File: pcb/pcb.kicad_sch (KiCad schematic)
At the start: 46 parts, among them J1 Conn_02x08_Top_Bottom, J2 Conn_02x08_Top_Bottom, SW1 CherryMX_LED, SW2 CherryMX_LED, SW3 1241.1100.7095, SW4 SW_SPST, U1 ICM7211AMIPL, U2 ICM7211AMIPL, U3 ATTINY84A, U4 NL37WZ14USG, U5 SN74AHC138DR, U6 MAX5035BUSA+, U6 SN74F02D, U7 TC7WZ32FK_LJCT, Y1 Crystal

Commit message: initialize pcb design
Signed-off-by: Michael Darr <michael.e.darr@gmail.com>
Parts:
- BT1: value Battery -> ~9V; footprint (none) -> Connector_Wire:SolderWire-0.15sqmm_1x02_P4mm_D0.5mm_OD1.5mm; Capacity ~5Ah -> (none); Cells 6 * AAA -> (none); Manufacturer_Name (none) -> Memory Protection Devices, Inc; Notes (none) -> 6 AAA batteries, ~9Ah; PN (none) -> BH26AAAW; Volatage ~12V -> (none)
- C1, C2, C3, C4, C5, C6, C7: footprint (none) -> chess_clock:RDER71H104K0M1H03A; Capacitance (none) -> 0.1µF; Manufacturer_Name (none) -> Murata; Notes (none) -> Ceramic Capacitor; PN (none) -> RDER71H104K0M1H03A
- C10: value C -> 0.1µF; footprint (none) -> chess_clock:RDER71H104K0M1H03A; Manufacturer_Name (none) -> Murata; Notes datasheet, pg 12: "Use a 1µF or greater value ceramic capac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 -> Ceramic Capacitor; PN (none) -> RDER71H104K0M1H03A; Type ceramic -> (none)
- C11: renamed from C7; value C -> 0.1µF; footprint (none) -> chess_clock:RDER71H104K0M1H03A; Manufacturer_Name (none) -> Murata; Notes (none) -> Ceramic Capacitor; PN (none) -> RDER71H104K0M1H03A; Spec page 9: "Bypass VD to GND with a 0.1µF ceramic capacitor." -> (none); Type ceramic -> (none)
- C12: renamed from C6; value C_Polarized_Small_US -> 68µF; footprint (none) -> chess_clock:TPSD686K010R0100; Manufacturer_Name (none) -> KYOCERA AVX; Notes (none) -> Polarized Capacitor; PN (none) -> TPSD686K010R0100
- C13: renamed from C11; value C -> 11pF; footprint (none) -> chess_clock:GJM1555C1H110FB01D; Capacitance 20pF -> 11pF; Manufacturer_Name (none) -> Murata; Notes (none) -> Ceramic Capacitor; PN (none) -> GJM1555C1H110FB01D
- C14: renamed from C12; value C -> 11pF; footprint (none) -> chess_clock:GJM1555C1H110FB01D; Capacitance 20pF -> 11pF; Manufacturer_Name (none) -> Murata; Notes (none) -> Ceramic Capacitor; PN (none) -> GJM1555C1H110FB01D
- C8: value C -> 0.1µF; footprint (none) -> chess_clock:RDER71H104K0M1H03A; Manufacturer_Name (none) -> Murata; Notes (none) -> Ceramic Capacitor; PN (none) -> RDER71H104K0M1H03A; Spec pg. 9: "Connect a 0.1µF ceramic capacitor from BST to LX." -> (none); Type ceramic -> (none)
- C9: value C_Polarized_Small_US -> 68µF; footprint (none) -> chess_clock:TPSD686K010R0100; Manufacturer_Name (none) -> KYOCERA AVX; Notes TODO => calculate precise capacitance (pg. 11/12) -> Polarized Capacitor; PN (none) -> TPSD686K010R0100
- D1: value D_Schottky -> Schottky Diode; footprint (none) -> chess_clock:B240AE-13; Manufacturer_Name (none) -> Diodes Inc.; Notes (none) -> Schottky Diode | page 11, table 1, 7.5 to 36; PN (none) -> B240AE-13; PN - Central Semiconductor B240 -> (none); PN - Diodes, Inc B240A -> (none); PN - IR 15MQ040N -> (none); PN - ON Semiconductor MBRS240, MBRS1540 -> (none); Spec page 11, table 1, 7.5 to 36 (PN recommendations reproduced 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 -> (none)
- FET1, FET2: value XP9561GI -> PMOS; footprint (none) -> Package_TO_SOT_THT:TO-220-3_Vertical; Manufacturer_Name (none) -> Yageo; PN (none) -> XP9561GI
- J1, J2: value Conn_02x08_Top_Bottom -> Dubugging Headers; footprint (none) -> chess_clock:10129381-916001BLF; Manufacturer_Name (none) -> Amphenol; PN (none) -> 10129381-916001BLF
- L1: value L -> 100μH; footprint (none) -> chess_clock:DO5022P-104MLD; Inductance 100μH -> (none); Manufacturer_Name (none) -> Coilcraft; PN (none) -> DO5022P-104MLD
- LCD1, LCD2: footprint DIP4000W30P254L6985H218Q40N -> chess_clock:LCD-S401C71TR; Arrow Part Number LCD-S401C71TR -> (none); Arrow Price/Stock https://www.arrow.com/en/products/lcd-s401c71tr/lumex -> (none); Height 2.18 -> (none); Manufacturer_Part_Number LCD-S401C71TR -> (none); Mouser Part Number 696-LCD-S401C71TR -> (none); Mouser Price/Stock https://www.mouser.co.uk/ProductDetail/Lumex/LCD-S401C71TR?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 -> (none); PN (none) -> LCD-S401C71TR
- LED1: value 151033RS03000 -> Red low battery Indicator; footprint (none) -> LED_THT:LED_D3.0mm_Clear; Manufacturer_Name (none) -> Wurth Elektronik; PN (none) -> 151033RS03000
- LS1: footprint (none) -> chess_clock:CT-1205H-SMT; Manufacturer_Name (none) -> CUI Devices; PN (none) -> CT-1205H-SMT-TR
- R1, R2, R3: footprint (none) -> Resistor_THT:R_Axial_DIN0204_L3.6mm_D1.6mm_P2.54mm_Vertical; Manufacturer_Name (none) -> TE connectivity; PN (none) -> ROX1SJ100R
- R4: footprint (none) -> Resistor_THT:R_Axial_DIN0204_L3.6mm_D1.6mm_P2.54mm_Vertical; Manufacturer_Name (none) -> TE connectivity; PN (none) -> CFR16J4K7
- R5: footprint (none) -> Resistor_THT:R_Axial_DIN0204_L3.6mm_D1.6mm_P2.54mm_Vertical; Manufacturer_Name (none) -> TE connectivity; PN (none) -> CFR50J5K6
- R6, R7, R8: footprint (none) -> Resistor_THT:R_Axial_DIN0204_L3.6mm_D1.6mm_P2.54mm_Vertical; Manufacturer_Name (none) -> TE connectivity; PN (none) -> ROX1SJ100K
- SW1, SW2: value CherryMX_LED -> Cherry MX Grey Switch w/ Green LED; footprint (none) -> chess_clock:MX_LED; Manufacturer_Name (none) -> Cherry; Notes (none) -> LED PN: INL-3AG30 [datasheet](https://www.inolux-corp.com/d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; PN (none) -> MX1A-D1NA
- SW3: footprint (none) -> chess_clock:MCS 18 Front; Manufacturer_Name (none) -> Schurter; PN (none) -> 1241.1100.7095
- SW4: footprint (none) -> chess_clock:CWSA11AAN1H; Manufacturer_Name (none) -> NKK Switches; PN (none) -> CWSA11AAN1H
- U1, U2: value ICM7211AMIPL -> Display Driver; footprint 21-0044B_40_MXM -> chess_clock:ICM7211AMIPL; Manufacturer_Name (none) -> Maxim; PN (none) -> ICM7211AMIPL
- U3: value ATTINY84A -> MCU; footprint DIP794W56P254L1918H533Q14N -> chess_clock:ATtiny84a; Height 5.334 -> (none); Manufacturer_Part_Number ATTINY48A-PU -> (none); PN (none) -> ATTINY84A
- U4: value NL37WZ14USG -> Inverter, 3 Channels; footprint US8_2P40X2P10_ONS -> chess_clock:NL37WZ14USG; Manufacturer_Name (none) -> Onsemi; PN (none) -> NL37WZ14USG
- U5: value SN74AHC138DR -> 3:8 Demux; footprint D16 -> chess_clock:SN74AHC138DR; Manufacturer_Name (none) -> Texas Instruments; PN (none) -> SN74AHC138DR
- U6: value SN74F02D -> NOR, 4 Channels; footprint D14 -> chess_clock:SN74F02D; Manufacturer_Name (none) -> Texas Instruments; PN (none) -> SN74F02D
- U7: value TC7WZ32FK_LJCT -> OR, 2 Channels; footprint US8_TOS -> chess_clock:TC7WZ32FK_LJCT; Manufacturer_Name (none) -> Toshiba; PN (none) -> TC7WZ32FK
- U8: renamed from U6; value MAX5035BUSA+ -> 5V Buck Voltage Regulator; footprint 21-0041B_8_MXM -> chess_clock:MAX5035BUSA+; Manufacturer_Name (none) -> Maxim; PN (none) -> MAX5035BUSA+
- Y1: value Crystal -> 20MHz Crystal; footprint (none) -> chess_clock:ECS_200_18_4X_CKM; Frequency 20MHz -> (none); Manufacturer_Name (none) -> ECS Inc; PN (none) -> ECS-200-18-4X-CKM
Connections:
- net GND: now also C1.1, C2.1, C3.1, SW1.1; no longer C1.2, C2.2, C3.2, SW1.2
- net VCC: now also C1.2, C2.2, C3.2; no longer C1.1, C2.1, C3.1
- net buzz: now also LS1.1 (-), U5.12 (Y3)
- net at R6.1: now also SW1.2; no longer SW1.1
- net col1_disable renamed ~{col1_enable}
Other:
- note removed: "0.5"
- note removed: "12/11/23"
- note removed: "Cn decouples Un"
- note removed: "liclock"
- company: (none) -> Alset
- title: (none) -> Liclock
- moved on the sheet: BT1, C1, C10, C11, C12, C13, C14, C2, C3, C4, C5, C6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
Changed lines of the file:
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@@
 (kicad_sch (version 20230121) (generator eeschema)
   (paper "A4")
+  (title_block
+    (title "Liclock")
+    (date "2023-12-12")
+    (rev "0,6")
+    (company "Alset")
+  )

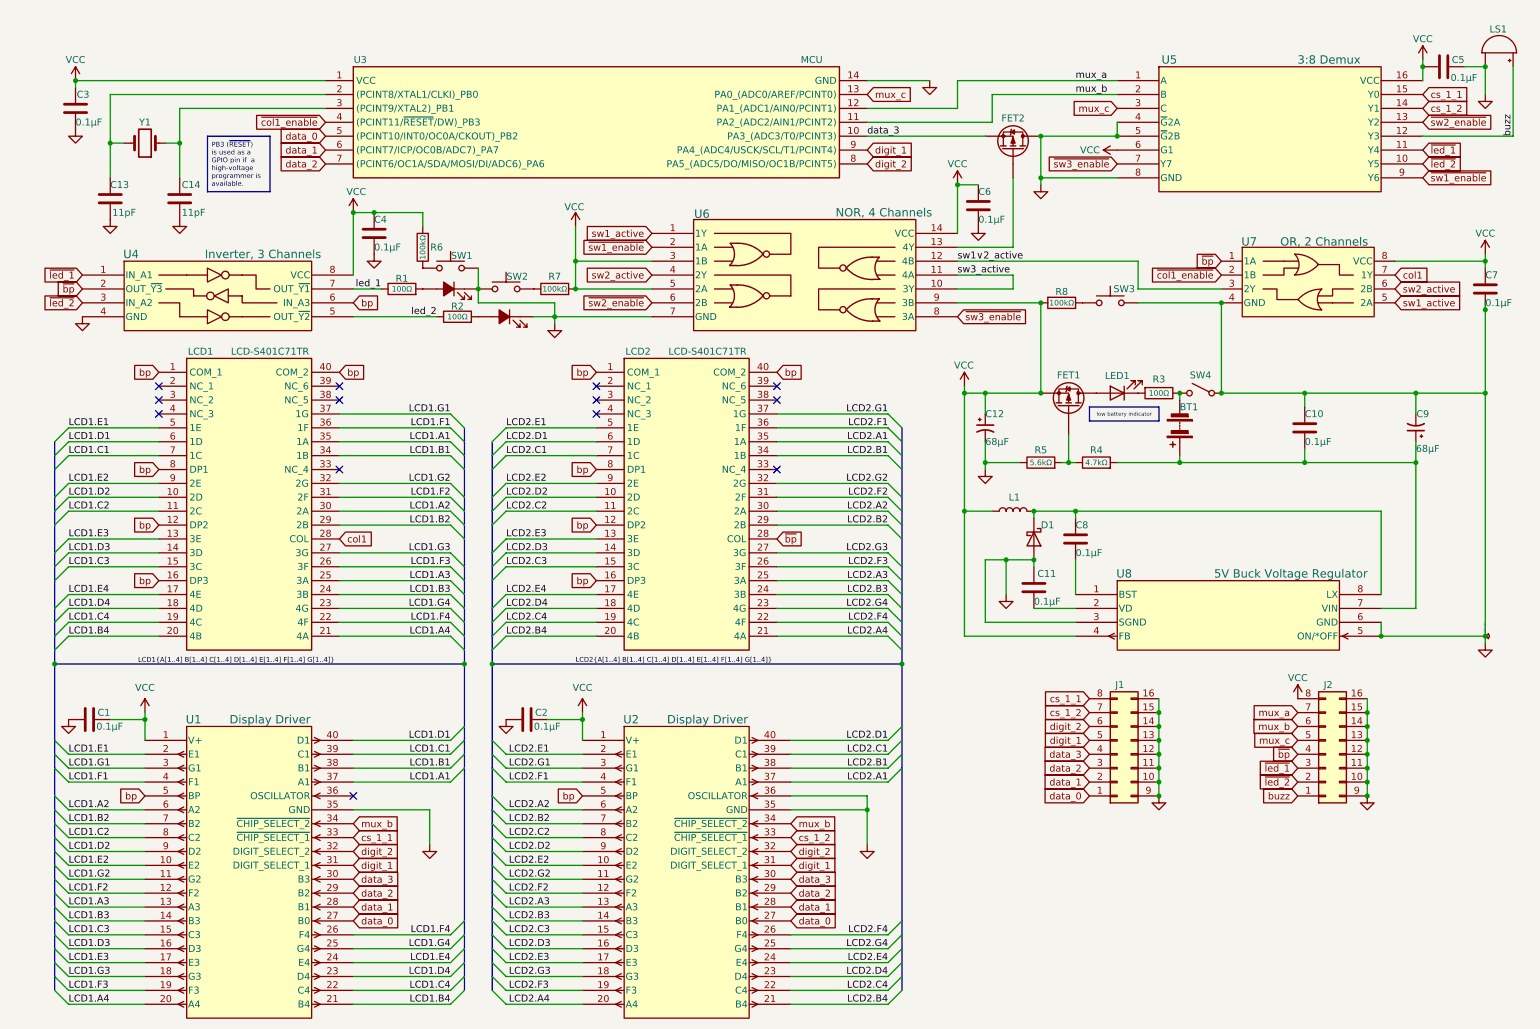
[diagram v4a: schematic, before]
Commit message: begin split pcb layout
Signed-off-by: Michael Darr <michael.e.darr@gmail.com>
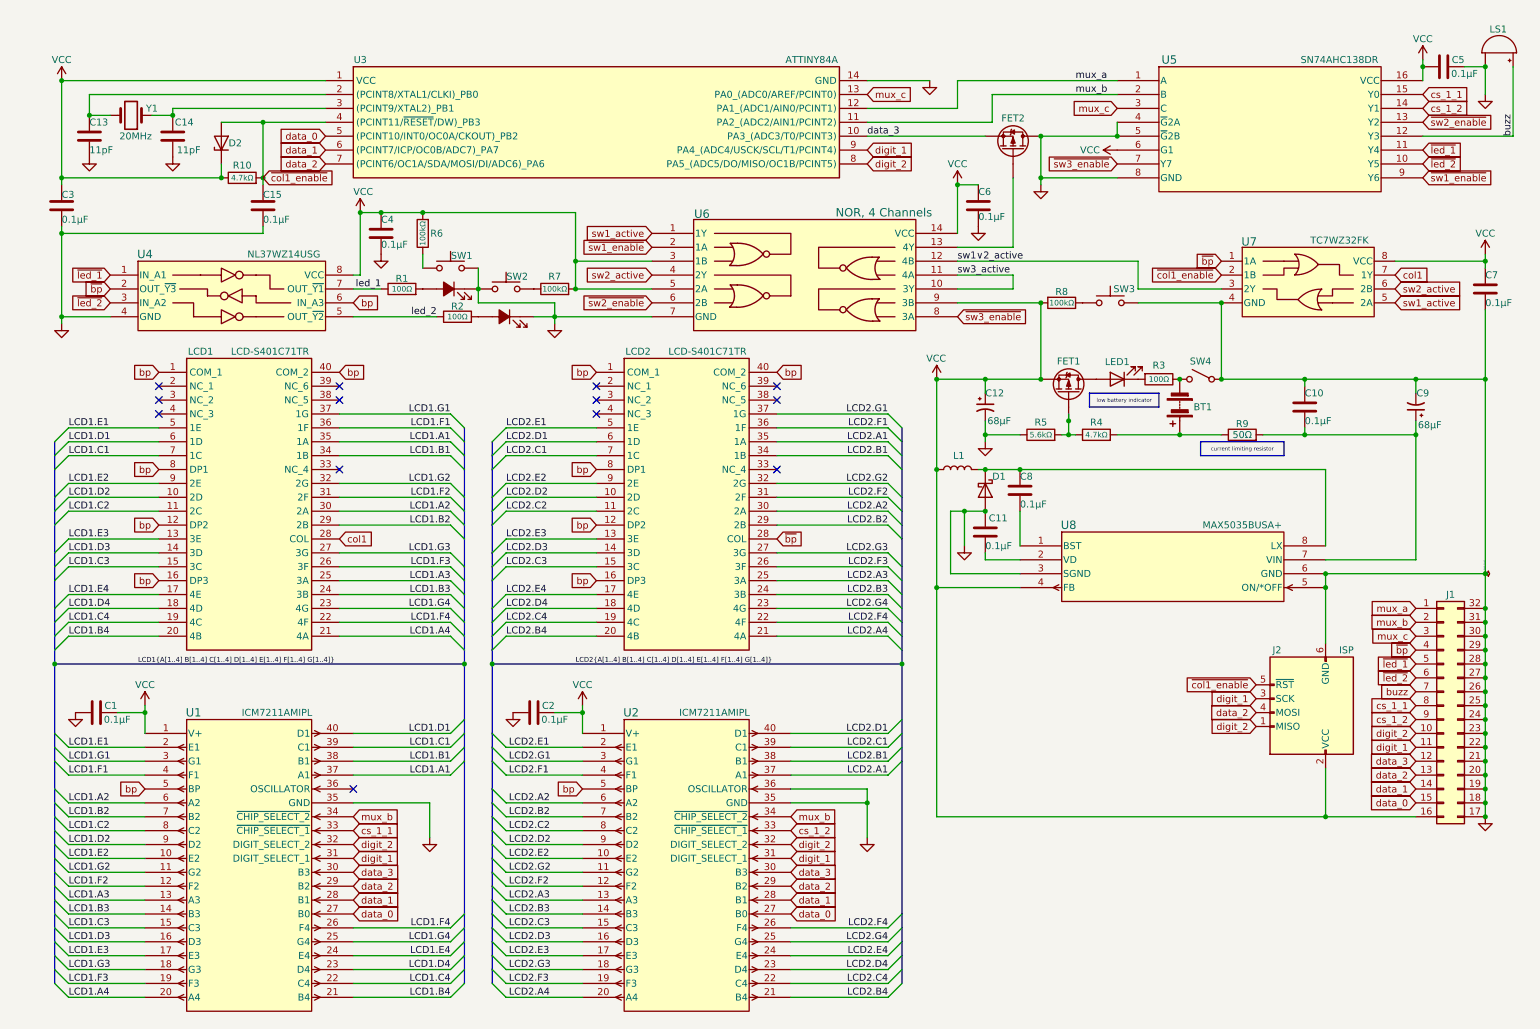
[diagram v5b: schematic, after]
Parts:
- removed J1, J2: Dubugging Headers, chess_clock:10129381-916001BLF, symbol Connector_Generic:Conn_02x08_Top_Bottom
- added C15: 0.1µF, chess_clock:RDER71H104K0M1H03A, symbol Device:C
- added D2: TVS Diode, Diode_SMD:D_SOD-523, symbol Device:D_Zener
- added J1: Debugging, Connector_PinHeader_2.54mm:PinHeader_2x16_P2.54mm_Vertical, symbol Connector_Generic:Conn_02x16_Counter_Clockwise
- added J2: ISP, Connector_PinHeader_2.54mm:PinHeader_2x03_P2.54mm_Vertical, symbol Connector:AVR-ISP-6
- added R10: 4.7kΩ, Resistor_THT:R_Axial_DIN0204_L3.6mm_D1.6mm_P2.54mm_Vertical, symbol Device:R
- added R9: 50Ω, chess_clock:352151RFT, symbol Device:R
- C1, C10, C11, C2, C3, C4, C5, C6, C7, C8: Capacitance 0.1µF -> (none); Notes Ceramic Capacitor -> (none)
- C12, C9: Capacitance 68µF -> (none); Notes Polarized Capacitor -> (none)
- C13, C14: Capacitance 11pF -> (none); Notes Ceramic Capacitor -> (none)
- D1: Notes Schottky Diode | page 11, table 1, 7.5 to 36 -> (none)
- Y1: value 20MHz Crystal -> 20MHz
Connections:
- net GND: now also C15.1, J1.17 (Pin_17), J1.18 (Pin_18), J1.19 (Pin_19), J1.20 (Pin_20), J1.21 (Pin_21), J1.22 (Pin_22), J1.23 (Pin_23), J1.24 (Pin_24), J1.25 (Pin_25), J1.26 (Pin_26), J1.27 (Pin_27), J1.28 (Pin_28), J1.29 (Pin_29), J1.30 (Pin_30), J1.31 (Pin_31), J1.32 (Pin_32), J2.6 (GND)
- net VCC: now also D2.1 (K), J1.16 (Pin_16), J2.2 (VCC), R10.1
- net buzz: now also J1.7 (Pin_7)
- net cs_1_1: now also J1.8 (Pin_8)
- net cs_1_2: now also J1.9 (Pin_9)
- net data_0: now also J1.15 (Pin_15)
- net data_1: now also J1.14 (Pin_14)
- net data_2: now also J1.13 (Pin_13), J2.4 (MOSI)
- net data_3: now also J1.12 (Pin_12)
- net digit_1: now also J1.11 (Pin_11), J2.3 (SCK)
- net digit_2: now also J1.10 (Pin_10), J2.1 (MISO)
- net mux_a: now also J1.1 (Pin_1)
- net mux_b: now also J1.2 (Pin_2)
- net mux_c: now also J1.3 (Pin_3)
- net ~{bp}: now also J1.4 (Pin_4)
- net ~{col1_enable}: now also C15.2, D2.2 (A), J2.5 (~{RST}), R10.2
- net ~{led_1}: now also J1.5 (Pin_5)
- net ~{led_2}: now also J1.6 (Pin_6)
- net at C10.2, C9.1, U8.7 (VIN): now also R9.2; no longer BT1.1 (+), R4.2
- new net: BT1.1 (+), R4.2, R9.1
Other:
- moved on the sheet: BT1, C1, C10, C11, C12, C13, C14, C2, C3, C4, C8, C9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

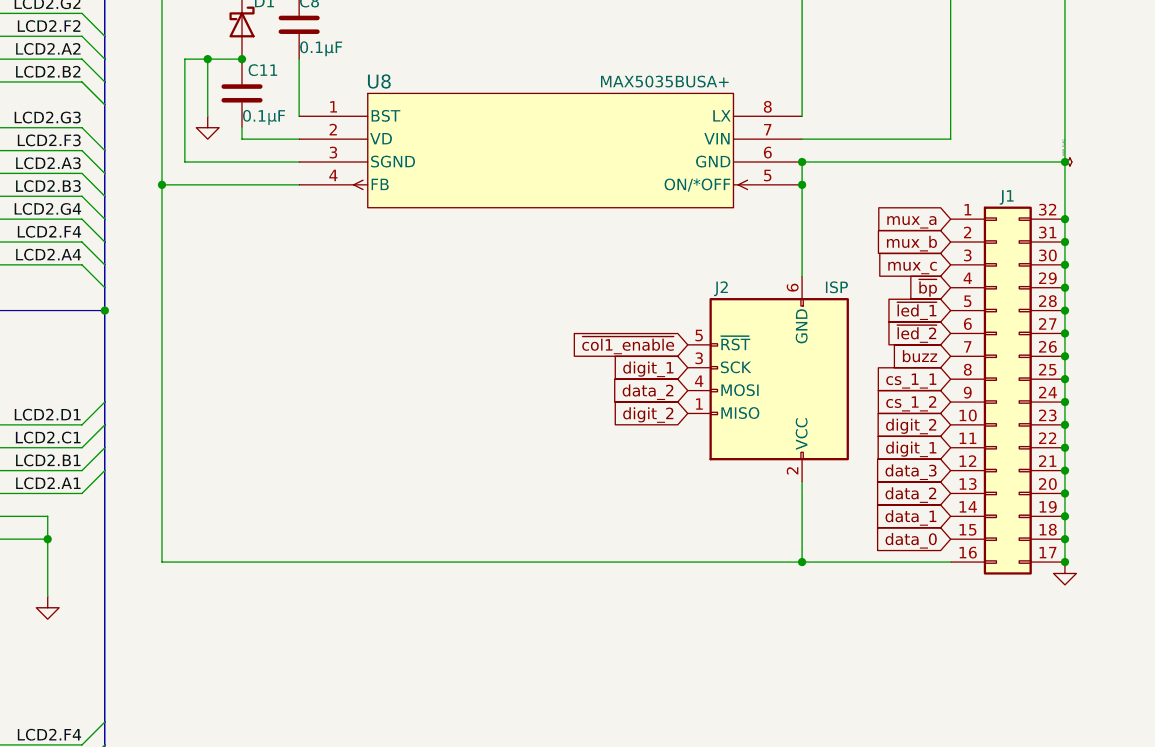
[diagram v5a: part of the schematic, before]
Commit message: Finish basic pcb layout
Signed-off-by: Michael Darr <michael.e.darr@gmail.com>
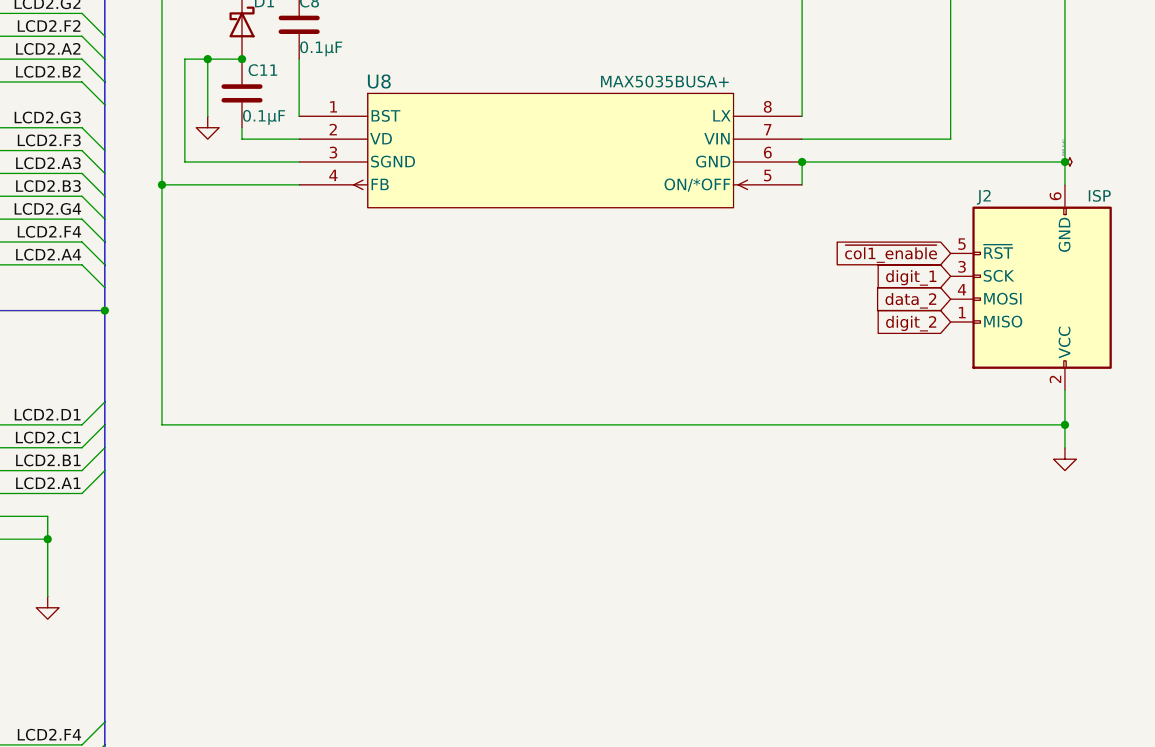
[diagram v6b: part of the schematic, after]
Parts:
- removed J1: Debugging, Connector_PinHeader_2.54mm:PinHeader_2x16_P2.54mm_Vertical, symbol Connector_Generic:Conn_02x16_Counter_Clockwise
- C1, C10, C11, C15, C2, C3, C4, C5, C6, C7, C8: footprint chess_clock:RDER71H104K0M1H03A -> chess_clock:GRM033R60J104KE19D; PN RDER71H104K0M1H03A -> GRM033R60J104KE19D
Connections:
- net VCC is gone; now on net GND: C1.2, C12.1, C2.2, C3.2, C4.1, C5.1, C6.1, C7.1, D2.1 (K), FET1.3 (S), J2.2 (VCC), L1.1, R10.1, R6.2, R7.2, R8.2, U1.1 (V+), U2.1 (V+), U3.1 (VCC), U4.8 (VCC), U5.16 (VCC), U5.6 (G1), U6.14 (VCC), U6.3 (1B), U6.5 (2A), U6.9 (3B), U7.8 (VCC), U8.4 (FB)
- net GND: no longer C10.1, C7.2, C9.2, J2.6 (GND), SW3.2, SW4.1 (A), U7.4 (GND), U8.5 (ON/*OFF), U8.6 (GND)
- new net: C10.1, C7.2, C9.2, J2.6 (GND), SW3.2, SW4.1 (A), U7.4 (GND), U8.5 (ON/*OFF), U8.6 (GND)
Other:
- moved on the sheet: J2
